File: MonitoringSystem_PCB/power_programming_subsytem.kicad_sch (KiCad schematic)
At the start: 12 parts, among them J6 USB_B, Q1 SS8050-G, Q2 SS8050-G, U1 CP2102N-Axx-xQFN28, U6 LM1117MP-3.3

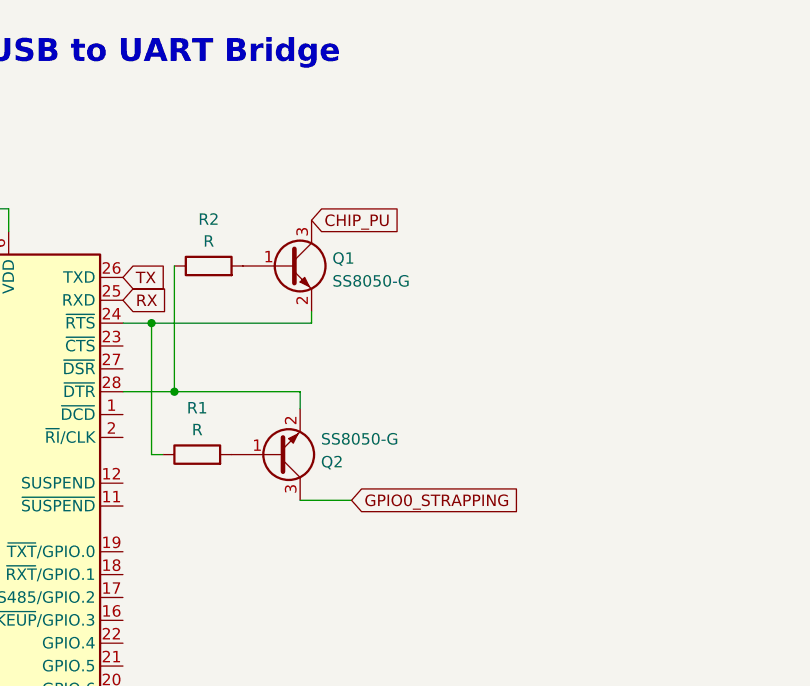
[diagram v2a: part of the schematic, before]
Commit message: minor change to usb-uart bridge
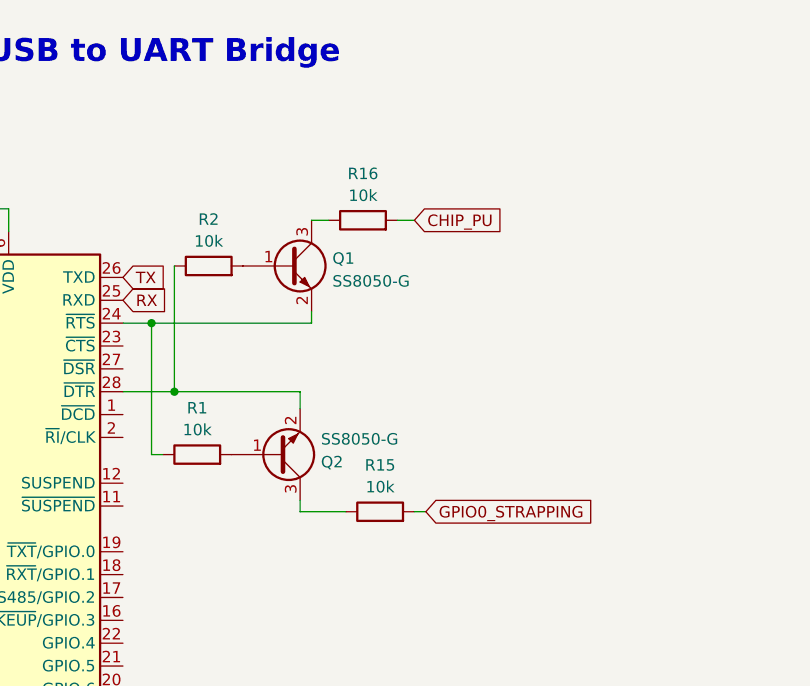
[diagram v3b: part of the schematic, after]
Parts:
- added R15, R16: 10k, Resistor_SMD:R_0805_2012Metric, symbol Device:R
- R1, R2: value R -> 10k
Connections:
- net CHIP_PU: now also R16.2; no longer Q1.3 (C)
- net GPIO0_STRAPPING: now also R15.2; no longer Q2.3 (C)
- new net: Q2.3 (C), R15.1
- new net: Q1.3 (C), R16.1
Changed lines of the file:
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@@
+	(wire
+		(pts
+			(xy 132.715 154.305) (xy 133.985 154.305)
+		)
+		(stroke
+			(width 0)
+			(type default)
+		)
+	)
 	(wire
 		(pts
@@
 	(wire
 		(pts
+			(xy 120.015 154.305) (xy 125.095 154.305)
+		)
+		(stroke
+			(width 0)
+			(type default)
+		)
+	)
+	(wire
+		(pts
 			(xy 106.045 127) (xy 106.045 140.97)
 		)
@@
 	(wire
 		(pts
+			(xy 130.81 121.92) (xy 132.715 121.92)
+		)
+		(stroke
+			(width 0)
+			(type default)
+		)
+	)
+	(wire
+		(pts
 			(xy 69.85 116.84) (xy 69.85 120.65)
 		)
@@
 	(wire
 		(pts
+			(xy 121.285 121.92) (xy 123.19 121.92)
+		)
+		(stroke
+			(width 0)
+			(type default)
+		)
+	)
+	(wire
+		(pts
 			(xy 55.245 140.97) (xy 55.245 142.24)
 		)
@@
 	(wire
 		(pts
-			(xy 125.73 153.035) (xy 120.015 153.035)
-		)
-		(stroke
-			(width 0)
-			(type default)
-		)
-	)
-	(wire
-		(pts
 			(xy 69.85 120.65) (xy 85.09 120.65)
 		)
@@
 		(pts
 			(xy 102.235 52.705) (xy 120.015 52.705)
+		)
+		(stroke
+			(width 0)
+			(type default)
+		)
+	)
+	(wire
+		(pts
+			(xy 120.015 154.305) (xy 120.015 153.035)
 		)
 		(stroke
@@
 	(global_label "CHIP_PU"
 		(shape input)
-		(at 121.285 121.92 0)
+		(at 132.715 121.92 0)
 		(fields_autoplaced yes)
 		(effects
@@
 		)
 		(property "Intersheetrefs" "${INTERSHEET_REFS}"
-			(at 132.3136 121.92 0)
+			(at 143.7436 121.92 0)
 			(effects
 				(font
@@
 	(global_label "GPIO0_STRAPPING"
 		(shape input)
-		(at 125.73 153.035 0)
+		(at 133.985 154.305 0)
 		(fields_autoplaced yes)
 		(effects
@@
 		)
 		(property "Intersheetrefs" "${INTERSHEET_REFS}"
-			(at 145.6486 153.035 0)
+			(at 153.9036 154.305 0)
 			(effects
 				(font
@@
 	)
 	(symbol
+		(lib_id "Device:R")
+		(at 128.905 154.305 90)
+		(unit 1)
+		(exclude_from_sim no)
+		(in_bom yes)
+		(on_board yes)
+		(dnp no)
+		(property "Reference" "R15"
+			(at 128.905 149.1445 90)
+			(effects
+				(font
+					(size 1.27 1.27)
+				)
+			)
+		)
+		(property "Value" "10k"
+			(at 128.905 151.5688 90)
+			(effects
+				(font
+					(size 1.27 1.27)
+				)
+			)
+		)
+		(property "Footprint" "Resistor_SMD:R_0805_2012Metric"
+			(at 128.905 156.083 90)
+			(effects
+				(font
+					(size 1.27 1.27)
+				)
+				(hide yes)
+			)
+		)
+		(property "Datasheet" "~"
+			(at 128.905 154.305 0)
+			(effects
+				(font
+					(size 1.27 1.27)
+				)
+				(hide yes)
+			)
+		)
+		(property "Description" "Resistor"
+			(at 128.905 154.305 0)
+			(effects
+				(font
+					(size 1.27 1.27)
+				)
+				(hide yes)
+			)
+		)
+		(pin "1"
+		)
+		(pin "2"
+		)
+		(instances
+			(project "MonitoringSystem_PCB"
+				(path "/e63e39d7-6ac0-4ffd-8aa3-1841a4541b55/6009ba97-19f7-4ca6-b0d1-715a2fb0321a"
+					(reference "R15")
+					(unit 1)
+				)
+			)
+		)
+	)
+	(symbol
 		(lib_id "Device:C_Small")
 		(at 43.18 144.78 0)
@@
 			)
 		)
-		(property "Value" "R"
+		(property "Value" "10k"
 			(at 108.585 145.2188 90)
 			(effects
@@
 	)
 	(symbol
+		(lib_id "Device:R")
+		(at 127 121.92 90)
+		(unit 1)
+		(exclude_from_sim no)
+		(in_bom yes)
+		(on_board yes)
+		(dnp no)
+		(fields_autoplaced yes)
+		(property "Reference" "R16"
+			(at 127 116.7595 90)
+			(effects
+				(font
+					(size 1.27 1.27)
+				)
+			)
+		)
+		(property "Value" "10k"
+			(at 127 119.1838 90)
+			(effects
+				(font
+					(size 1.27 1.27)
+				)
+			)
+		)
+		(property "Footprint" "Resistor_SMD:R_0805_2012Metric"
+			(at 127 123.698 90)
+			(effects
+				(font
+					(size 1.27 1.27)
+				)
+				(hide yes)
+			)
+		)
+		(property "Datasheet" "~"
+			(at 127 121.92 0)
+			(effects
+				(font
+					(size 1.27 1.27)
+				)
+				(hide yes)
+			)
+		)
+		(property "Description" "Resistor"
+			(at 127 121.92 0)
+			(effects
+				(font
+					(size 1.27 1.27)
+				)
+				(hide yes)
+			)
+		)
+		(pin "1"
+		)
+		(pin "2"
+		)
+		(instances
+			(project "MonitoringSystem_PCB"
+				(path "/e63e39d7-6ac0-4ffd-8aa3-1841a4541b55/6009ba97-19f7-4ca6-b0d1-715a2fb0321a"
+					(reference "R16")
+					(unit 1)
+				)
+			)
+		)
+	)
+	(symbol
 		(lib_id "Device:Q_NPN_BEC")
 		(at 118.745 127 0)
@@
 			)
 		)
-		(property "Value" "R"
+		(property "Value" "10k"
 			(at 109.855 124.2638 90)
 			(effects

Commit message: pcb done
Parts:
- added C2: 4.7 uF, Capacitor_SMD:C_0805_2012Metric, symbol Device:C_Small
- added C29: 0.1 uF, Capacitor_SMD:C_0805_2012Metric, symbol Device:C_Small
- added R17: 4.7k, Resistor_SMD:R_0805_2012Metric, symbol Device:R
- C1: value 4.7 uF -> 1.0 uF
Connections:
- net +3.3V: now also C1.1, C3.1, U1.6 (VDD), U1.7 (VREGIN), C2.1, C29.1, R17.2
- net +5V: no longer C1.1, C3.1, U1.6 (VDD), U1.7 (VREGIN)
- net GND: now also C2.2, C29.2
- net at U1.9 (~{RST}): now also R17.1
- no-connect marks 1 -> 17

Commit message: finalized pcb, fixed eroors, generated gerber
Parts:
- removed J6: USB_B, USB-B:CUI_UJ2-BH-W1-TH, symbol Connector:USB_B
- added J2: UJ2-BH-W1-TH, USB-B:CUI_UJ2-BH-W1-TH, symbol USB-B:UJ2-BH-W1-TH
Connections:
- net GND: now also J2.4 (GND), J2.SH1 (SHIELD), J2.SH2 (SHIELD__1)
- net USB_D+: now also D1.1 (A1), J2.3 (D+); no longer D2.1 (A1)
- net USB_D-: now also D2.1 (A1), J2.2 (D-); no longer D1.1 (A1)
- net at D3.2 (A): now also J2.1 (VBUS)
- no-connect marks 17 -> 16
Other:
- moved on the sheet: D1, D2

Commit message: BOM and minor pcb updates
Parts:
- C1: value 1.0 uF -> 1 uF
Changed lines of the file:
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@@
 			)
 		)
-		(property "Value" "1.0 uF"
+		(property "Value" "1 uF"
 			(at 67.0941 118.6934 0)
 			(effects

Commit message: most recent pcb
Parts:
- removed D1, D2: SZESD9B5.0ST5G, Diode_SMD:D_SOD-923, symbol Diode:SZESD9B5.0ST5G
- removed U1: CP2102N-Axx-xQFN28, Package_DFN_QFN:QFN-28-1EP_5x5mm_P0.5mm_EP3.35x3.35mm, symbol Interface_USB:CP2102N-Axx-xQFN28
- added C30, C31: 10 uF, Capacitor_SMD:C_0805_2012Metric, symbol Device:C_Small
- added D1, D2, D4: SMAJ5.0CA, Diode_SMD:D_SMA, symbol Diode:SMAJ5.0CA
- added D5: PWR_IND, LED_SMD:LED_0805_2012Metric, symbol Device:LED
- added J6: Conn_01x05_Female, Connector_PinHeader_2.54mm:PinHeader_1x05_P2.54mm_Vertical, symbol Connector:Conn_01x05_Female
- added R18: 1k, Resistor_SMD:R_0805_2012Metric, symbol Device:R
- added U4: CP2102N-Axx-xQFN24, Package_DFN_QFN:QFN-24-1EP_4x4mm_P0.5mm_EP2.6x2.6mm, symbol Interface_USB:CP2102N-Axx-xQFN24
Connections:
- net +3.3V: now also C31.1, U4.5 (VIO), U4.6 (VDD), U4.7 (VREGIN)
- net +5V: now also C30.1, R18.1, U4.8 (VBUS)
- net GND: now also C30.2, C31.2, D1.2 (A2), D2.2 (A2), D4.2 (A2), D5.1 (K), J6.5 (Pin_5), U4.2 (GND), U4.25 (GND)
- net RX: now also J6.4 (Pin_4), U4.20 (RXD)
- net TX: now also J6.3 (Pin_3), U4.21 (TXD)
- net USB_D+: now also D1.1 (A1), U4.3 (D+)
- net USB_D-: now also D4.1 (A1), U4.4 (D-)
- net DTR: now reaches Q2.2 (E), R2.1
- net DTR: now also J6.2 (Pin_2), U4.23 (~{DTR})
- net at R17.1: now also U4.9 (~{RST})
- net RTS: now reaches Q1.2 (E), R1.1
- net RTS: now also J6.1 (Pin_1), U4.19 (~{RTS})
- net at D3.2 (A), J2.1 (VBUS): now also D2.1 (A1)
- new net: D5.2 (A), R18.2
- no-connect marks 16 -> 10
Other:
- note added: "Programming Circuit"
- note removed: "Micro-USB to UART Bridge"
- moved on the sheet: D3, Q1, Q2, R1, R15, R16, R2
